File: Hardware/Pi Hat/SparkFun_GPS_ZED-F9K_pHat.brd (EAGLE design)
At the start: 65 x 56.5 mm, 92 parts, among them J1 QWIIC_RIGHT_ANGLE, J2 RASPBERRYPI-40-PIN-GPIO_PTH_N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, J4 U.FL, U1 UBLOX_ZED_F9R

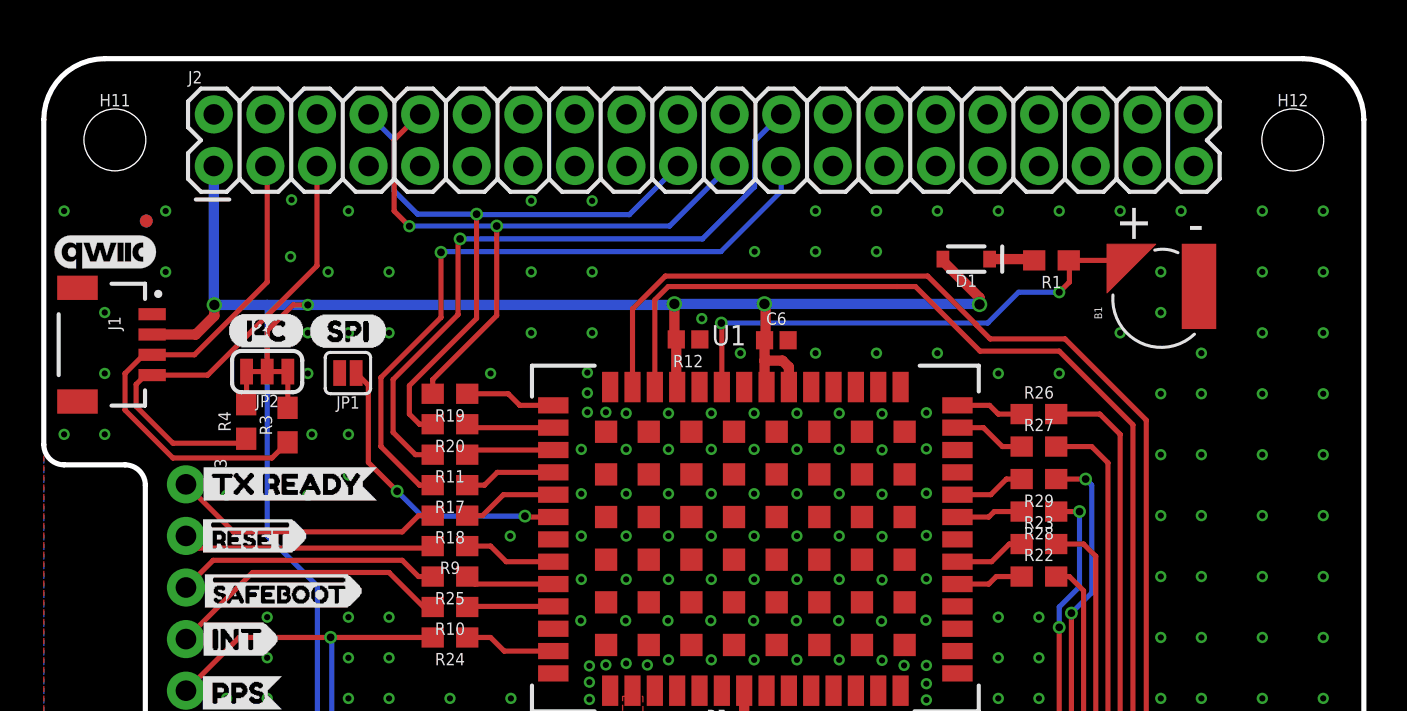
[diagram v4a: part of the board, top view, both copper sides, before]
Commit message: Changes PTH header to double SMD male/femail combination
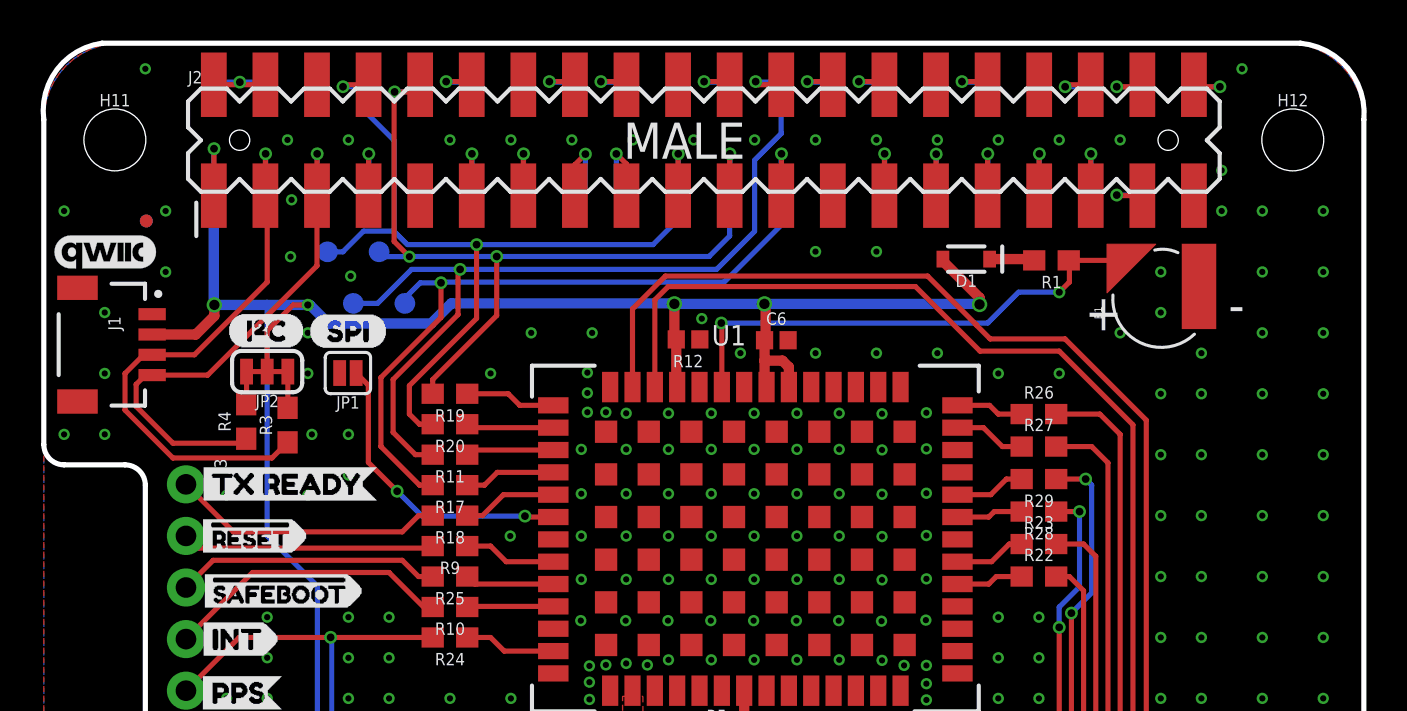
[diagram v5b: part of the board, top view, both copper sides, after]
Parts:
- added TP1, TP2, TP3, TP4: TEST-POINT3X4, SparkFun-Connectors:PAD.03X.04
- J2: value RASPBERRYPI-40-PIN-GPIO_PTH_NO_SHROUD -> RASPBERRYPI-40-PIN-GPIO_SMD_STACK_NOHOLES_NOREF; device SparkFun-Connectors:2X20 -> SparkFun-Connectors:RASPBERRY_PI_HAT_40_PIN_SMD_STACKABLE_NOHOLES_NOREF
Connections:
- new net CE1: J2.26, J2.26B
- new net GP12: J2.32, J2.32B
- new net GP13: J2.33, J2.33B
- new net GP16: J2.36, J2.36B
- new net GP17: J2.11, J2.11B
- new net GP18: J2.12, J2.12B
- new net GP19: J2.35, J2.35B
- new net GP20: J2.38, J2.38B
- new net GP21: J2.40, J2.40B
- new net GP22: J2.15, J2.15B
- new net GP23: J2.16, J2.16B
- new net GP24: J2.18, J2.18B
- new net GP25: J2.22, J2.22B
- new net GP26: J2.37, J2.37B
- new net GP27: J2.13, J2.13B
- new net GP4: J2.7, J2.7B
- new net GP5: J2.29, J2.29B
- new net GP6: J2.31, J2.31B
- new net ID_SC: J2.28, J2.28B
- new net ID_SD: J2.27, J2.27B
- net 3.3V: now also J2.17B, J2.1B
- net 5V: now also J2.2B, J2.4B
- net GND: now also J2.14B, J2.20B, J2.25B, J2.30B, J2.34B, J2.39B, J2.6B, J2.9B
- net QWIIC_SCL: now also J2.5B
- net QWIIC_SDA: now also J2.3B
- net RXI/MOSI: now also J2.19B, J2.8B, TP1.P$1
- net SCL/CLK: now also J2.23B, TP3.P$1
- net SDA/!CS: now also J2.24B, TP4.P$1
- net TXO/MISO: now also J2.10B, J2.21B, TP2.P$1
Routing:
- net RXI/MOSI: track 32.3 -> 45.4 mm, vias 1 -> 3
- net SDA/!CS: track 33.0 -> 43.5 mm, vias 1 -> 2
- net TXO/MISO: track 32.9 -> 43.4 mm, vias 2 -> 4
- net 3.3V: track 109.4 -> 117.8 mm, vias 6 -> 8
- net 5V: track 0.00 -> 5.26 mm, vias 0 -> 1
- net SCL/CLK: track 33.4 -> 38.5 mm, vias 1 -> 2
- net GP22: track 0.00 -> 4.65 mm, vias 0 -> 1
- net GP27: track 0.00 -> 4.26 mm, vias 0 -> 1
- net GP17: track 0.00 -> 4.26 mm, vias 0 -> 1
- net ID_SD: track 0.00 -> 4.26 mm, vias 0 -> 1
- net GP6: track 0.00 -> 4.26 mm, vias 0 -> 1
- net GP4: track 0.00 -> 4.26 mm, vias 0 -> 1
- net GP19: track 0.00 -> 4.26 mm, vias 0 -> 1
- net GP13: track 0.00 -> 4.26 mm, vias 0 -> 1
- net GP5: track 0.00 -> 4.23 mm, vias 0 -> 1
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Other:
- board size 65 x 56.5 mm -> 65 x 57.3 mm

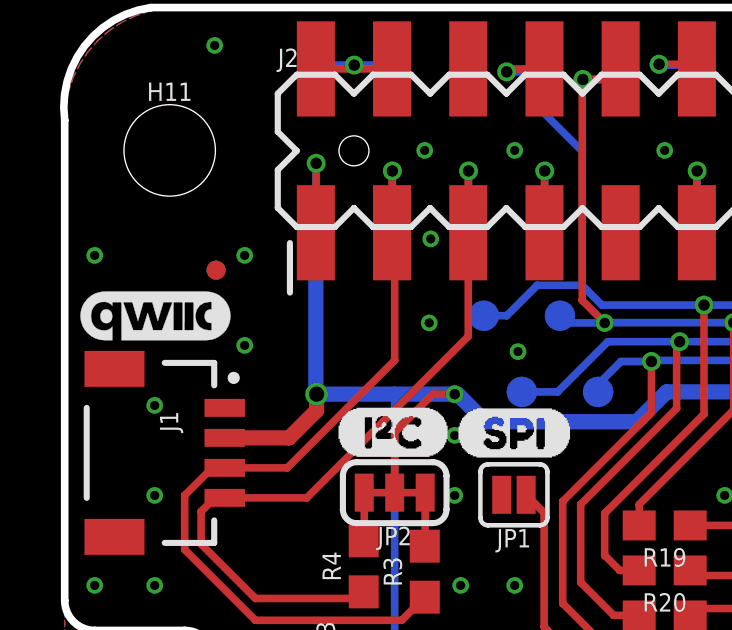
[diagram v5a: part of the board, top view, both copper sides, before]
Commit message: Adds test point for power
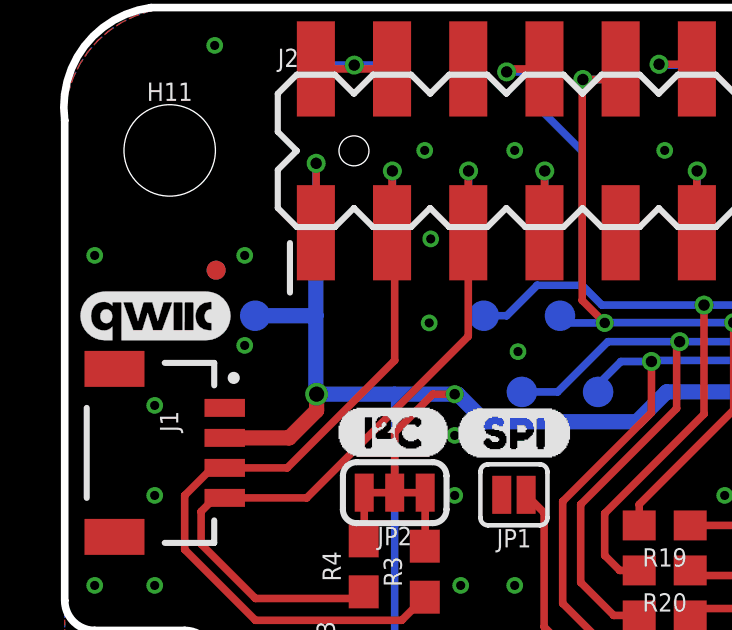
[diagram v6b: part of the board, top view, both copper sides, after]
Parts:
- added TP5: TEST-POINT3X4, SparkFun-Connectors:PAD.03X.04
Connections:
- net 3.3V: now also TP5.P$1
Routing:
- net 3.3V: track 117.8 -> 119.8 mm
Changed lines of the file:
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@@
 <setting verticaltext="up"/>
 </settings>
-<grid distance="0.05" unitdist="inch" unit="inch" style="lines" multiple="1" display="yes" altdistance="0.01" altunitdist="inch" altunit="inch"/>
+<grid distance="0.05" unitdist="inch" unit="mm" style="lines" multiple="1" display="yes" altdistance="0.005" altunitdist="inch" altunit="mm"/>
 <layers>
 <layer number="1" name="Top" color="4" fill="1" visible="yes" active="yes"/>
@@
 <layer number="115" name="ReferenceISLANDS" color="7" fill="1" visible="no" active="no"/>
 <layer number="116" name="Patch_BOT" color="9" fill="4" visible="no" active="no"/>
-<layer number="117" name="PM_Ref" color="26" fill="1" visible="no" active="yes"/>
+<layer number="117" name="PM_Ref" color="26" fill="1" visible="yes" active="yes"/>
 <layer number="118" name="Rect_Pads" color="7" fill="1" visible="no" active="no"/>
-<layer number="119" name="PF_Ref" color="31" fill="1" visible="no" active="yes"/>
-<layer number="120" name="WFL_Ref" color="25" fill="1" visible="no" active="yes"/>
+<layer number="119" name="PF_Ref" color="31" fill="1" visible="yes" active="yes"/>
+<layer number="120" name="WFL_Ref" color="25" fill="1" visible="yes" active="yes"/>
 <layer number="121" name="_tsilk" color="7" fill="1" visible="no" active="no"/>
 <layer number="122" name="_bsilk" color="7" fill="1" visible="no" active="no"/>
@@
 <element name="TP3" library="SparkFun-Connectors" package="PAD.03X.04" value="TEST-POINT3X4" x="17.78" y="44.45" smashed="yes" rot="MR270"/>
 <element name="TP4" library="SparkFun-Connectors" package="PAD.03X.04" value="TEST-POINT3X4" x="15.24" y="44.45" smashed="yes" rot="MR270"/>
+<element name="TP5" library="SparkFun-Connectors" package="PAD.03X.04" value="TEST-POINT3X4" x="6.35" y="46.99" smashed="yes" rot="MR0"/>
 </elements>
 <signals>
@@
 <contactref element="J2" pad="17B"/>
 <wire x1="8.3974" y1="44.3744" x2="8.372" y2="44.3998" width="0.508" layer="16"/>
-<wire x1="8.372" y1="44.3998" x2="8.372" y2="49.6285" width="0.508" layer="16"/>
+<wire x1="8.372" y1="44.3998" x2="8.372" y2="46.99" width="0.508" layer="16"/>
+<wire x1="8.372" y1="46.99" x2="8.372" y2="49.6285" width="0.508" layer="16"/>
 <wire x1="8.372" y1="49.6285" x2="8.372" y2="52.06" width="0.254" layer="16"/>
 <wire x1="8.372" y1="52.06" x2="8.382" y2="52.07" width="0.254" layer="16"/>
@@
 <wire x1="20.062" y1="44.45" x2="31.026" y2="44.45" width="0.508" layer="16"/>
 <wire x1="31.026" y1="44.45" x2="31.0508" y2="44.4252" width="0.508" layer="16"/>
+<contactref element="TP5" pad="P$1"/>
+<wire x1="8.372" y1="46.99" x2="6.35" y2="46.99" width="0.508" layer="16"/>
 <wire x1="31.0508" y1="44.4252" x2="28.692" y2="49.6285" width="0" layer="19" extent="16-16"/>
 </signal>
@@
 <wire x1="9.984" y1="39.5032" x2="9.984" y2="41.092" width="0.254" layer="1"/>
 </signal>
-<signal name="RF_IN">
+<signal name="RF_IN" class="1">
 <contactref element="J4" pad="FEED"/>
 <wire x1="29" y1="22.9362" x2="29" y2="8.4378" width="1" layer="1"/>

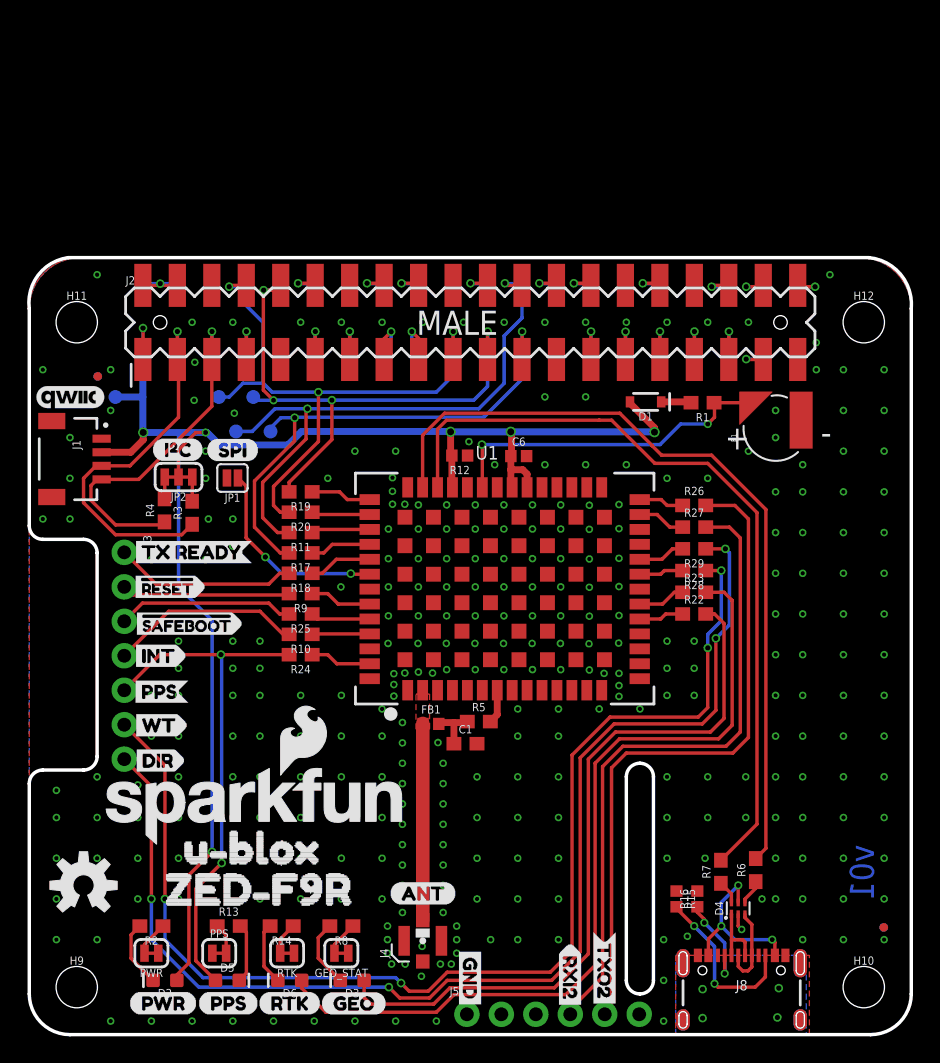
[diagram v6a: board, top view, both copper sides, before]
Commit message: Adds wheel tick and direction circuit to pi-hat
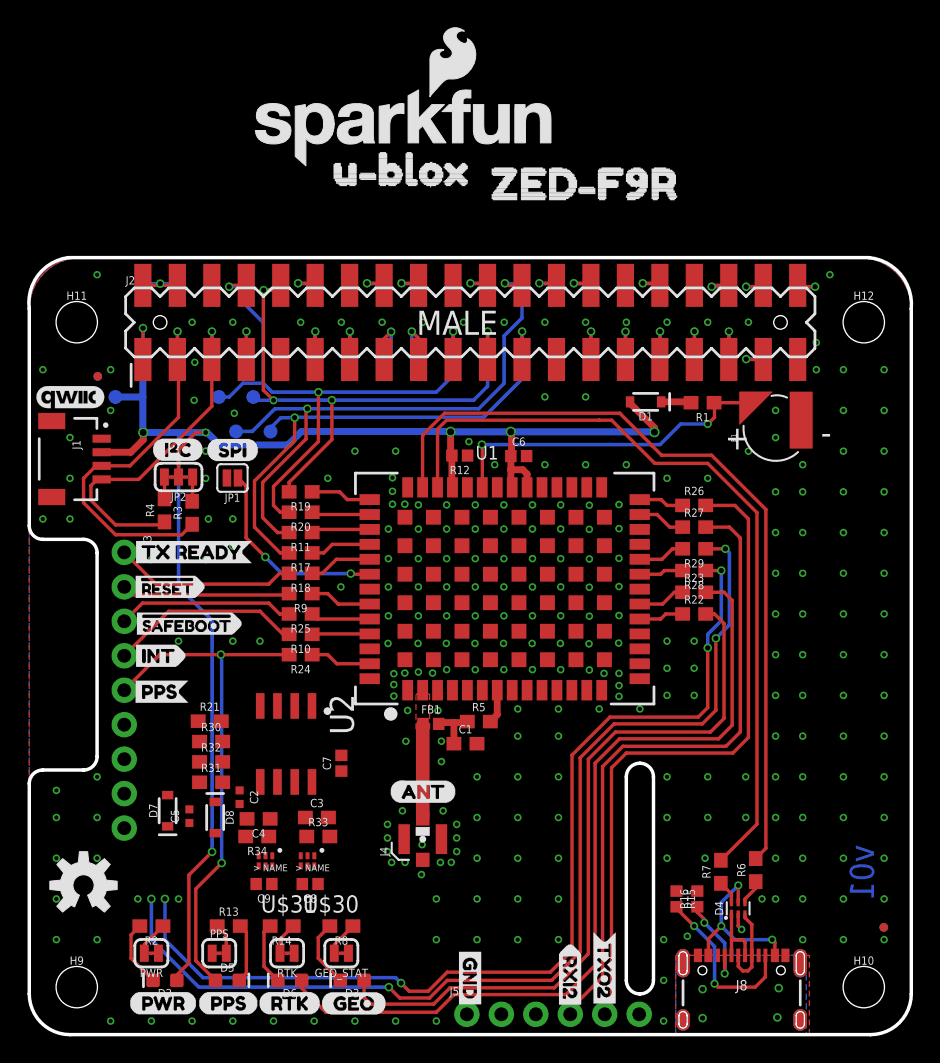
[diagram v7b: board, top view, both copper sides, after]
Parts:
- removed U$22: (no value), wt_dir:DIR1
- removed U$23: (no value), wt_dir:WT0
- removed U$27: (no value), wt_dir:DIR3
- removed U$28: (no value), wt_dir:WT2
- added C2, C5: 1.0nF, SparkFun-Capacitors:0402-TIGHT
- added C3, C4: 22nF, SparkFun-Capacitors:0603
- added C7, C8, C9: 0.1uF, SparkFun-Capacitors:0402
- added D7, D8: 0.5A/40V/420mV, SparkFun-DiscreteSemi:SOD-323
- added R21, R31: 3.3k, SparkFun-Resistors:0603
- added R30, R32: 470, SparkFun-Resistors:0603
- added R33, R34: 910, classified:0603
- added U$30, U$31: UHS_INVERTER_SCHMITT_TRIGGERSIP6, classified:SIP6
- added U2: HCPL-270L, classified:SOP_8-PIN
- J3: device SparkFun-Connectors:1X07_NO_SILK -> SparkFun-Connectors:1X09_NO_SILK
- moved U$26 57.3 mm to (32.0, 62.7)
- moved U$25 51.2 mm to (20.3, 63.7)
- moved LOGO1 51.2 mm to (27.6, 66.8)
- moved J4 7.49 mm to (29.0, 14.4)
- moved U$21 7.49 mm to (26.5, 17.9)
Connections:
- removed net DIR: J3.7, R29.1
- removed net WT: J3.6, R28.1
- new net DIR+: J3.8, R31.1
- new net DIR-: C2.2, D8.A, J3.9, U2.P3
- new net DIR_IN: R32.2, U2.P4
- new net DIR_OUT: R29.1, U$31.P4
- new net DIR_SCHMITT: C4.1, R34.1, U$31.P2, U2.P6
- new net N$27: C5.1, D7.C, R21.2, R30.1
- new net N$36: C2.1, D8.C, R31.2, R32.1
- new net WT+: J3.6, R21.1
- new net WT-: C5.2, D7.A, J3.7, U2.P2
- new net WT_IN: R30.2, U2.P1
- new net WT_OUT: R28.1, U$30.P4
- new net WT_SCHMITT: C3.1, R33.1, U$30.P2, U2.P7
- net 3.3V: now also C7.1, C8.1, C9.1, R33.2, R34.2, U$30.P6, U$31.P6, U2.P8
- net GND: now also C3.2, C4.2, C7.2, C8.2, C9.2, U$30.P3, U$31.P3, U2.P5
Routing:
- net DIR: track 88.6 -> 0.00 mm, vias 4 -> 0
- net WT: track 87.4 -> 0.00 mm, vias 4 -> 0
- net DIR_OUT: track 0.00 -> 77.4 mm, vias 0 -> 4
- net WT_OUT: track 0.00 -> 73.3 mm, vias 0 -> 4
- net RF_IN: track 14.5 -> 6.88 mm
- net GND: vias 316 -> 265

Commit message: Routes wheel tick and direction circuitry
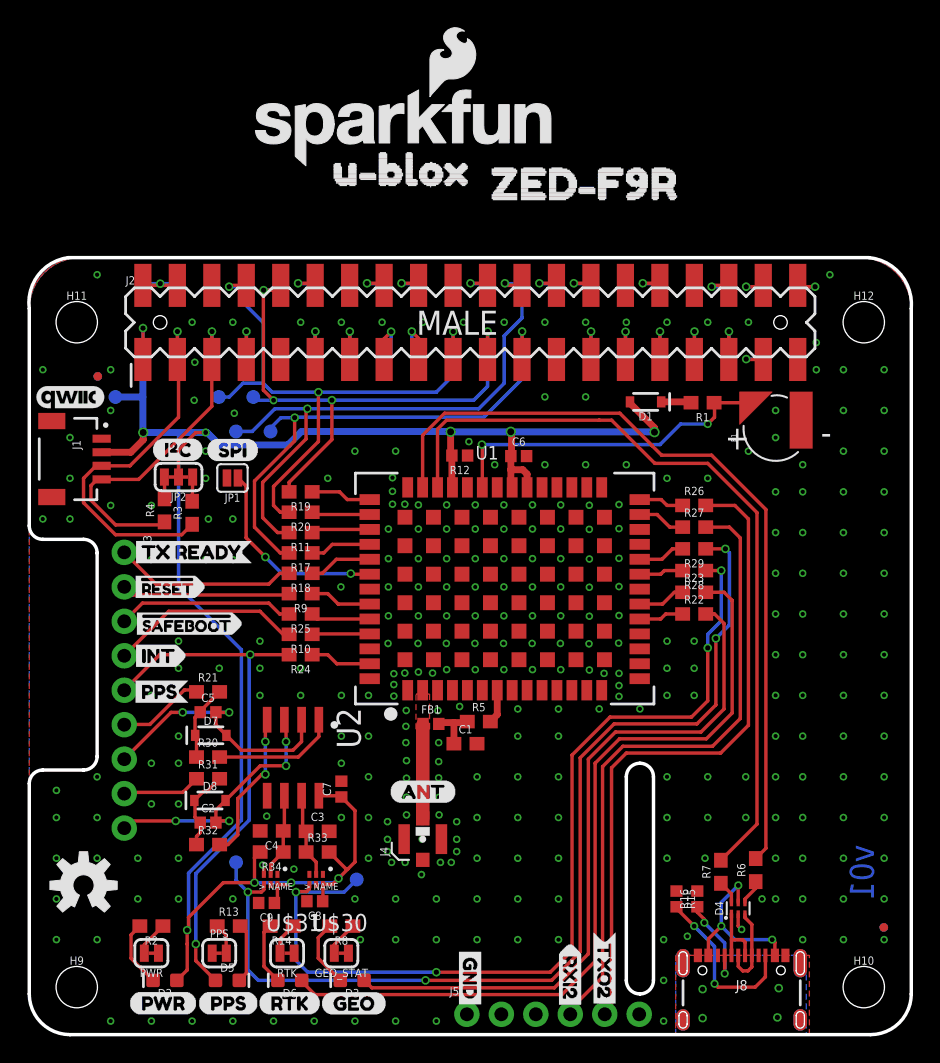
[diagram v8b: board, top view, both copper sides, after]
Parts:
- added TP6, TP7: TEST-POINT3X4, SparkFun-Connectors:PAD.03X.04
- C2, C5: device SparkFun-Capacitors:0402-TIGHT -> SparkFun-Capacitors:0402
- moved C5 7.78 mm to (13.2, 23.8), turned to 0 degrees
- moved D7 6.40 mm to (13.4, 22.1), turned to 0 degrees
- moved R32 6.10 mm to (13.2, 14.0)
- moved C2 2.98 mm to (13.2, 15.6), turned to 0 degrees
- moved R21 2.16 mm to (13.2, 25.3)
- moved C7 1.91 mm to (23.0, 18.1)
- moved R34 1.56 mm to (17.9, 13.5)
- moved U$30 1.51 mm to (21.1, 11.4)
- moved U$31 1.42 mm to (17.8, 11.4)
- moved C9 1.41 mm to (17.5, 9.70)
- moved C8 1.31 mm to (21.0, 9.83)
- moved D8 1.31 mm to (13.3, 17.3), turned to 0 degrees
- moved C4 1.31 mm to (17.9, 15.0)
- moved R30 1.16 mm to (13.2, 20.5)
- moved R33 1.14 mm to (21.2, 13.5)
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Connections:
- net DIR_OUT: now also TP7.P$1
- net WT_OUT: now also TP6.P$1
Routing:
- net 3.3V: track 119.8 -> 152.9 mm, vias 8 -> 11
- net WT-: track 0.00 -> 20.0 mm, vias 0 -> 2
- net DIR-: track 0.00 -> 19.9 mm, vias 0 -> 4
- net DIR_IN: track 0.00 -> 11.2 mm, vias 0 -> 2
- net WT_IN: track 0.00 -> 9.18 mm
- net WT+: track 0.00 -> 6.44 mm
- net WT_SCHMITT: track 0.00 -> 6.24 mm
- net DIR_SCHMITT: track 0.00 -> 6.21 mm
- net N$36: track 0.00 -> 6.08 mm
- net DIR+: track 0.00 -> 5.78 mm
- net N$27: track 0.00 -> 5.60 mm
- net WT_OUT: track 73.3 -> 69.9 mm
- net DIR_OUT: track 77.4 -> 75.0 mm
- net GEOF_STAT: track 53.8 -> 51.6 mm
- net RTK_STAT: track 61.9 -> 59.8 mm
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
